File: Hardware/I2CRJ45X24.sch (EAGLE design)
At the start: 129 parts, among them IC1 MCP23017SO, IC2 MCP23017SO, IC3 MCP23017SO, IC4 MCP23017SO, IC5 MCP23017SO, IC6 MCP23017SO, J1 I2C-BREAKOUT, J2 I2C-BREAKOUT, J3 M01-PLAIN, J4 RJ45-X8, J5 RJ45-X8, J6 RJ45-X8

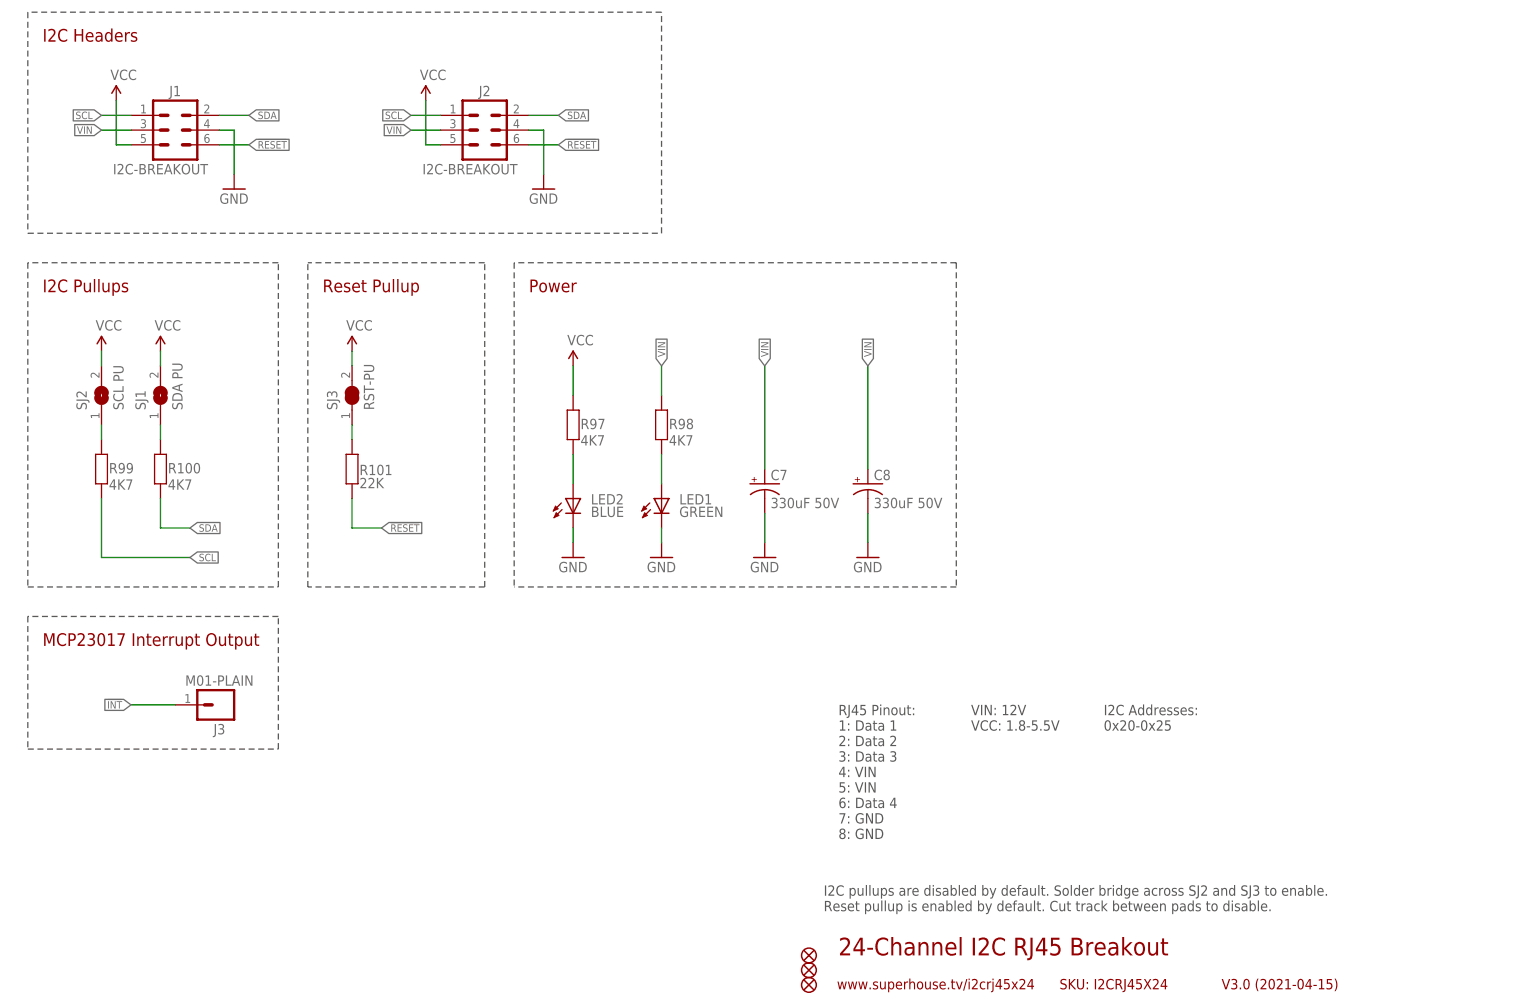
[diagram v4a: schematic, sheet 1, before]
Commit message: Major rework for v3.0 release of all versions.
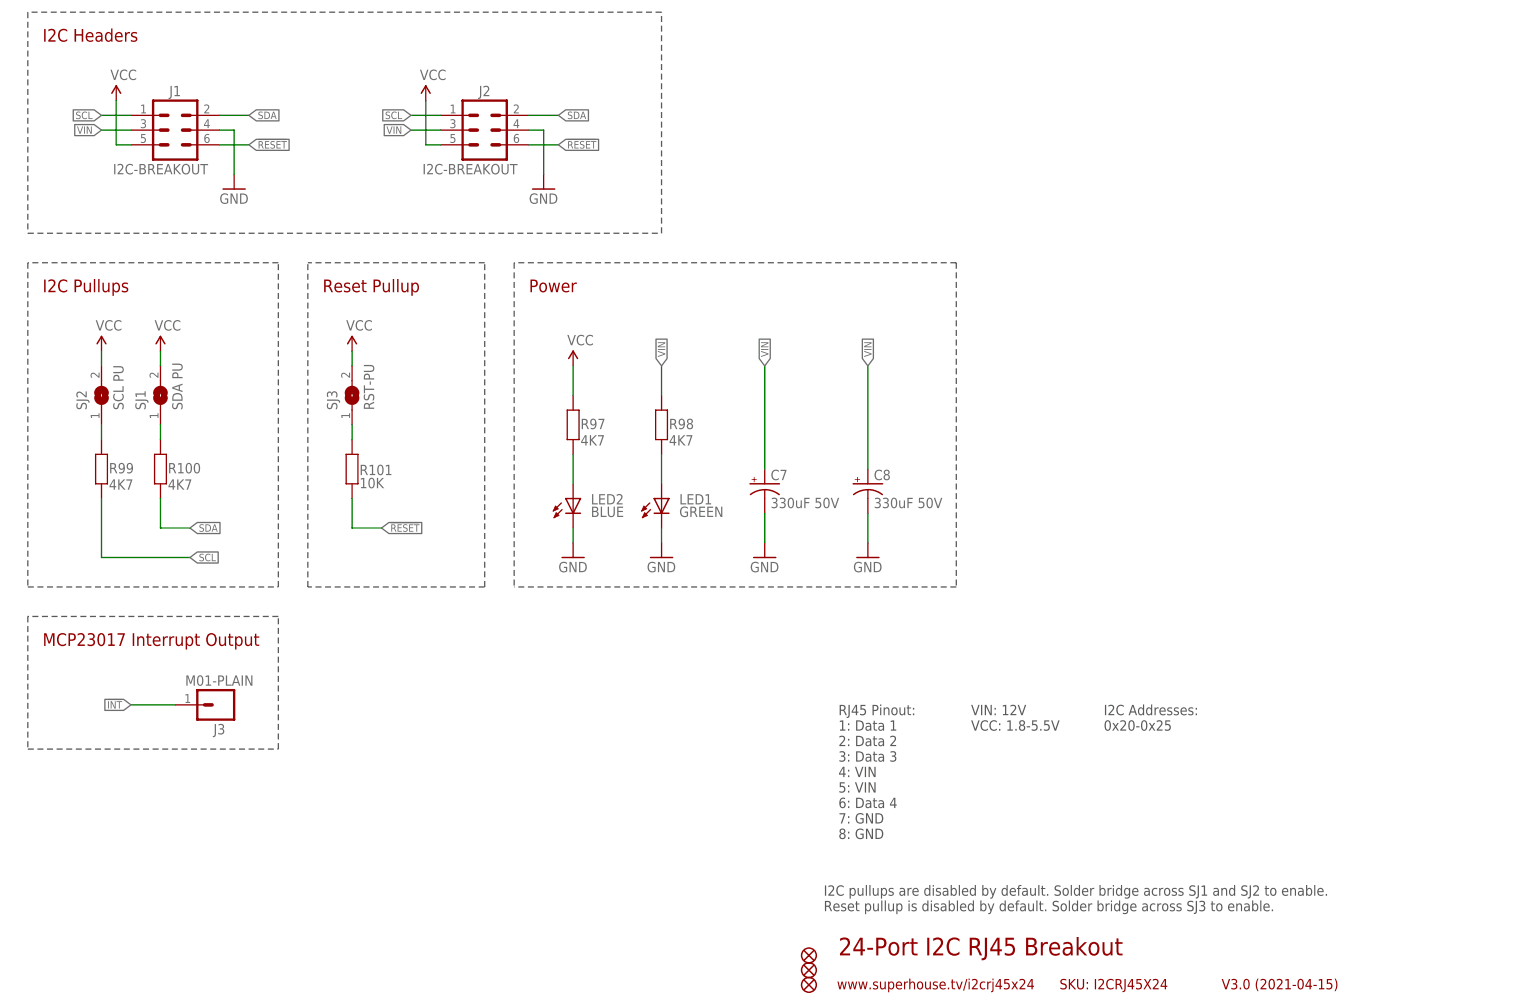
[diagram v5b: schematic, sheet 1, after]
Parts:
- R101: value 22K -> 10K
- SJ3: device SuperHouse-Jumpers:SJC-NORMAL -> SuperHouse-Jumpers:SJ-NORMAL
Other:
- note added: "24-Port I2C RJ45 Breakout"
- note added: "I2C pullups are disabled by default. Solder bridge across SJ1 and SJ2 to enable. Reset pullup is disabled by default. Solder bridge across SJ3 to enable."
- note removed: "24-Channel I2C RJ45 Breakout"
- note removed: "I2C pullups are disabled by default. Solder bridge across SJ2 and SJ3 to enable. Reset pullup is enabled by default. Cut track between pads to disable."
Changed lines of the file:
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@@
 <part name="C3" library="SuperHouse-DiscreteSemi" library_urn="urn:adsk.eagle:library:11768461" deviceset="CAP" device="0805" package3d_urn="urn:adsk.eagle:package:7066318/4" value="10uF"/>
 <part name="C4" library="SuperHouse-DiscreteSemi" library_urn="urn:adsk.eagle:library:11768461" deviceset="CAP" device="0805" package3d_urn="urn:adsk.eagle:package:7066318/4" value="10uF"/>
-<part name="SJ2" library="SuperHouse-Jumpers" library_urn="urn:adsk.eagle:library:12190622" deviceset="SJ" device="-NORMAL" package3d_urn="urn:adsk.eagle:package:7066338/1" value="SCL PU"/>
-<part name="SJ1" library="SuperHouse-Jumpers" library_urn="urn:adsk.eagle:library:12190622" deviceset="SJ" device="-NORMAL" package3d_urn="urn:adsk.eagle:package:7066338/1" value="SDA PU"/>
+<part name="SJ2" library="SuperHouse-Jumpers" library_urn="urn:adsk.eagle:library:12190622" deviceset="SJ" device="-NORMAL" package3d_urn="urn:adsk.eagle:package:7066338/2" value="SCL PU"/>
+<part name="SJ1" library="SuperHouse-Jumpers" library_urn="urn:adsk.eagle:library:12190622" deviceset="SJ" device="-NORMAL" package3d_urn="urn:adsk.eagle:package:7066338/2" value="SDA PU"/>
 <part name="P+8" library="SuperHouse-SupplySymbols" library_urn="urn:adsk.eagle:library:11790503" deviceset="VCC" device=""/>
 <part name="P+9" library="SuperHouse-SupplySymbols" library_urn="urn:adsk.eagle:library:11790503" deviceset="VCC" device=""/>
@@
 <part name="GND14" library="SuperHouse-SupplySymbols" library_urn="urn:adsk.eagle:library:11790503" deviceset="GND" device=""/>
 <part name="GND15" library="SuperHouse-SupplySymbols" library_urn="urn:adsk.eagle:library:11790503" deviceset="GND" device=""/>
-<part name="R101" library="SuperHouse-DiscreteSemi" library_urn="urn:adsk.eagle:library:11768461" deviceset="RESISTOR" device="0603" package3d_urn="urn:adsk.eagle:package:11768543/2" value="22K"/>
+<part name="R101" library="SuperHouse-DiscreteSemi" library_urn="urn:adsk.eagle:library:11768461" deviceset="RESISTOR" device="0603" package3d_urn="urn:adsk.eagle:package:11768543/2" value="10K"/>
 <part name="P+12" library="SuperHouse-SupplySymbols" library_urn="urn:adsk.eagle:library:11790503" deviceset="VCC" device=""/>
-<part name="SJ3" library="SuperHouse-Jumpers" library_urn="urn:adsk.eagle:library:12190622" deviceset="SJC" device="-NORMAL" package3d_urn="urn:adsk.eagle:package:7066342/2" value="RST-PU"/>
+<part name="SJ3" library="SuperHouse-Jumpers" library_urn="urn:adsk.eagle:library:12190622" deviceset="SJ" device="-NORMAL" package3d_urn="urn:adsk.eagle:package:7066338/2" value="RST-PU"/>
 </parts>
 <sheets>
@@
 <plain>
 <frame x1="0" y1="0" x2="248.92" y2="185.42" columns="8" rows="5" layer="94"/>
-<text x="149.86" y="12.7" size="3.048" layer="94">24-Channel I2C RJ45 Breakout</text>
+<text x="149.86" y="12.7" size="3.048" layer="94">24-Port I2C RJ45 Breakout</text>
 <text x="215.9" y="6.858" size="1.778" layer="94">V3.0 (2021-04-15)</text>
 <text x="149.606" y="6.858" size="1.778" layer="94">www.superhouse.tv/i2crj45x24</text>
@@
 <wire x1="119.38" y1="137.16" x2="119.38" y2="175.26" width="0.2032" layer="97" style="longdash"/>
 <wire x1="119.38" y1="175.26" x2="10.16" y2="175.26" width="0.2032" layer="97" style="longdash"/>
-<text x="147.32" y="20.32" size="1.778" layer="97">I2C pullups are disabled by default. Solder bridge across SJ2 and SJ3 to enable.
-Reset pullup is enabled by default. Cut track between pads to disable.</text>
+<text x="147.32" y="20.32" size="1.778" layer="97">I2C pullups are disabled by default. Solder bridge across SJ1 and SJ2 to enable.
+Reset pullup is disabled by default. Solder bridge across SJ3 to enable.</text>
 <wire x1="93.98" y1="132.08" x2="93.98" y2="76.2" width="0.2032" layer="97" style="longdash"/>
 <wire x1="170.18" y1="132.08" x2="93.98" y2="132.08" width="0.2032" layer="97" style="longdash"/>
@@
 <attribute name="VALUE" x="65.024" y="120.396" size="1.778" layer="96"/>
 </instance>
-<instance part="SJ3" gate="G$1" x="66.04" y="109.22" smashed="yes" rot="R90">
+<instance part="SJ3" gate="1" x="66.04" y="109.22" smashed="yes" rot="R90">
 <attribute name="NAME" x="63.5" y="106.68" size="1.778" layer="95" rot="R90"/>
 <attribute name="VALUE" x="69.85" y="106.68" size="1.778" layer="96" rot="R90"/>
@@
 <segment>
 <pinref part="P+12" gate="1" pin="VCC"/>
-<pinref part="SJ3" gate="G$1" pin="2"/>
+<pinref part="SJ3" gate="1" pin="2"/>
 <wire x1="66.04" y1="114.3" x2="66.04" y2="116.84" width="0.1524" layer="91"/>
 </segment>
@@
 <segment>
 <pinref part="R101" gate="G$1" pin="2"/>
-<pinref part="SJ3" gate="G$1" pin="1"/>
+<pinref part="SJ3" gate="1" pin="1"/>
 <wire x1="66.04" y1="101.6" x2="66.04" y2="104.14" width="0.1524" layer="91"/>
 </segment>

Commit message: Began replacement of discrete resistors with resistor arrays.
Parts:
- removed R1, R10, R11, R12, R13, R14, R15, R16, R2, R3, R4, R5, R6, R7, R8, R9: 1K, SuperHouse-DiscreteSemi:RESISTOR0603
- added RN1, RN2, RN3, RN4: 1K, SuperHouse-DiscreteSemi:4R-NCAY16
- added RN5, RN6, RN7, RN8: (no value), SuperHouse-DiscreteSemi:4R-NCAY16
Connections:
- net 1A1: now also RN1D.2, RN5D.1; no longer R1.2
- net 1A2: now also RN1C.2, RN5C.1; no longer R3.2
- net 1A3: now also RN1B.2, RN5B.1; no longer R2.2
- net 1A6: now also RN1A.2, RN5A.1; no longer R4.2
- net 1B1: now also RN3D.2, RN7D.1; no longer R15.2
- net 1B2: now also RN3C.2, RN7C.1; no longer R13.2
- net 1B3: now also RN3B.2, RN7B.1; no longer R11.2
- net 1B6: now also RN3A.2, RN7A.1; no longer R9.2
- net 1E1: now also RN2D.2, RN6D.1; no longer R7.2
- net 1E2: now also RN2C.2, RN6C.1; no longer R6.2
- net 1E3: now also RN2B.2, RN6B.1; no longer R5.2
- net 1E6: now also RN2A.2, RN6A.1; no longer R8.2
- net 1F1: now also RN4D.2, RN8D.1; no longer R16.2
- net 1F2: now also RN4C.2, RN8C.1; no longer R14.2
- net 1F3: now also RN4B.2, RN8B.1; no longer R12.2
- net 1F6: now also RN4A.2, RN8A.1; no longer R10.2
- net GPA0-1: now also RN1D.1; no longer R1.1
- net GPA1-1: now also RN1C.1; no longer R3.1
- net GPA2-1: now also RN1B.1; no longer R2.1
- net GPA3-1: now also RN1A.1; no longer R4.1
- net GPA4-1: now also RN2D.1; no longer R7.1
- net GPA5-1: now also RN2C.1; no longer R6.1
- net GPA6-1: now also RN2B.1; no longer R5.1
- net GPA7-1: now also RN2A.1; no longer R8.1
- net GPB0-1: now also RN3D.1; no longer R15.1
- net GPB1-1: now also RN3C.1; no longer R13.1
- net GPB2-1: now also RN3B.1; no longer R11.1
- net GPB3-1: now also RN3A.1; no longer R9.1
- net GPB4-1: now also RN4D.1; no longer R16.1
- net GPB5-1: now also RN4C.1; no longer R14.1
- net GPB6-1: now also RN4B.1; no longer R12.1
- net GPB7-1: now also RN4A.1; no longer R10.1
- net VCC: now also RN5A.2, RN5B.2, RN5C.2, RN5D.2, RN6A.2, RN6B.2, RN6C.2, RN6D.2, RN7A.2, RN7B.2, RN7C.2, RN7D.2, RN8A.2, RN8B.2, RN8C.2, RN8D.2
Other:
- moved on the sheet: C1, C2, IC1, IC2, J4, R17, R18, R19, R20, R21, R22, R23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

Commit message: Progress on converting resistors to arrays and adding pullups.
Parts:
- removed R17, R18, R19, R20, R21, R22, R23, R24, R25, R26, R27, R28, R29, R30, R31, R32, R33, R34, R35, R36, R37, R38, R41, R42, R43, R44, R45, R46, R47, R48, R49, R50, R51, R52, R53, R54, R55, R56, R57, R58, R59, R60, R61, R62, R63, R64, R65, R66: 1K, SuperHouse-DiscreteSemi:RESISTOR0603
- added RN10, RN11, RN12, RN17, RN18, RN19, RN20, RN25, RN26, RN27, RN28, RN9: 1K, SuperHouse-DiscreteSemi:4R-NCAY16
- added RN13, RN14, RN15, RN16, RN21, RN22, RN23, RN24, RN29, RN30, RN31, RN32: 10K, SuperHouse-DiscreteSemi:4R-NCAY16
- RN5, RN6, RN7, RN8: value (none) -> 10K
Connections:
- net 1C1: now also RN13D.1, RN9D.2; no longer R17.2
- net 1C2: now also RN13C.1, RN9C.2; no longer R19.2
- net 1C3: now also RN13B.1, RN9B.2; no longer R18.2
- net 1C6: now also RN13A.1, RN9A.2; no longer R20.2
- net 1D1: now also RN11D.2, RN15D.1; no longer R31.2
- net 1D2: now also RN11C.2, RN15C.1; no longer R29.2
- net 1D3: now also RN11B.2, RN15B.1; no longer R27.2
- net 1D6: now also RN11A.2, RN15A.1; no longer R25.2
- net 1G1: now also RN10D.2, RN14D.1; no longer R23.2
- net 1G2: now also RN10C.2, RN14C.1; no longer R22.2
- net 1G3: now also RN10B.2, RN14B.1; no longer R21.2
- net 1G6: now also RN10A.2, RN14A.1; no longer R24.2
- net 1H1: now also RN12D.2, RN16D.1; no longer R32.2
- net 1H2: now also RN12C.2, RN16C.1; no longer R30.2
- net 1H3: now also RN12B.2, RN16B.1; no longer R28.2
- net 1H6: now also RN12A.2, RN16A.1; no longer R26.2
- net 2A1: now also RN17D.2, RN21D.1; no longer R33.2
- net 2A2: now also RN17C.2, RN21C.1; no longer R35.2
- net 2A3: now also RN17B.2, RN21B.1; no longer R34.2
- net 2A6: now also RN17A.2, RN21A.1; no longer R36.2
- net 2B1: now also RN19D.2, RN23D.1; no longer R49.2
- net 2B2: now also RN19C.2, RN23C.1; no longer R47.2
- net 2B3: now also RN19B.2, RN23B.1; no longer R45.2
- net 2B6: now also RN19A.2, RN23A.1; no longer R43.2
- net 2C1: now also RN25D.2, RN29D.1; no longer R51.2
- net 2C2: now also RN25C.2, RN29C.1; no longer R53.2
- net 2C3: now also RN25B.2, RN29B.1; no longer R52.2
- net 2C6: now also RN25A.2, RN29A.1; no longer R54.2
- net 2D1: now also RN27D.2, RN31D.1; no longer R65.2
- net 2D2: now also RN27C.2, RN31C.1; no longer R63.2
- net 2D3: now also RN27B.2, RN31B.1; no longer R61.2
- net 2D6: now also RN27A.2, RN31A.1; no longer R59.2
- net 2E1: now also RN18D.2, RN22D.1; no longer R41.2
- net 2E2: now also RN18C.2, RN22C.1; no longer R38.2
- net 2E3: now also RN18B.2, RN22B.1; no longer R37.2
- net 2E6: now also RN18A.2, RN22A.1; no longer R42.2
- net 2F1: now also RN20D.2, RN24D.1; no longer R50.2
- net 2F2: now also RN20C.2, RN24C.1; no longer R48.2
- net 2F3: now also RN20B.2, RN24B.1; no longer R46.2
- net 2F6: now also RN20A.2, RN24A.1; no longer R44.2
- net 2G1: now also RN26D.2, RN30D.1; no longer R57.2
- net 2G2: now also RN26C.2, RN30C.1; no longer R56.2
- net 2G3: now also RN26B.2, RN30B.1; no longer R55.2
- net 2G6: now also RN26A.2, RN30A.1; no longer R58.2
- net 2H1: now also RN28D.2, RN32D.1; no longer R66.2
- net 2H2: now also RN28C.2, RN32C.1; no longer R64.2
- net 2H3: now also RN28B.2, RN32B.1; no longer R62.2
- net 2H6: now also RN28A.2, RN32A.1; no longer R60.2
- net GPA0-2: now also RN9D.1; no longer R17.1
- net GPA0-3: now also RN17D.1; no longer R33.1
- net GPA0-4: now also RN25D.1; no longer R51.1
- net GPA1-2: now also RN9C.1; no longer R19.1
- net GPA1-3: now also RN17C.1; no longer R35.1
- net GPA1-4: now also RN25C.1; no longer R53.1
- net GPA2-2: now also RN9B.1; no longer R18.1
- net GPA2-3: now also RN17B.1; no longer R34.1
- net GPA2-4: now also RN25B.1; no longer R52.1
- net GPA3-2: now also RN9A.1; no longer R20.1
- net GPA3-3: now also RN17A.1; no longer R36.1
- net GPA3-4: now also RN25A.1; no longer R54.1
- net GPA4-2: now also RN10D.1; no longer R23.1
- net GPA4-3: now also RN18D.1; no longer R41.1
- net GPA4-4: now also RN26D.1; no longer R57.1
- net GPA5-2: now also RN10C.1; no longer R22.1
- net GPA5-3: now also RN18C.1; no longer R38.1
- net GPA5-4: now also RN26C.1; no longer R56.1
- net GPA6-2: now also RN10B.1; no longer R21.1
- net GPA6-3: now also RN18B.1; no longer R37.1
- net GPA6-4: now also RN26B.1; no longer R55.1
- net GPA7-2: now also RN10A.1; no longer R24.1
- net GPA7-3: now also RN18A.1; no longer R42.1
- net GPA7-4: now also RN26A.1; no longer R58.1
- net GPB0-2: now also RN11D.1; no longer R31.1
- net GPB0-3: now also RN19D.1; no longer R49.1
- net GPB0-4: now also RN27D.1; no longer R65.1
- net GPB1-2: now also RN11C.1; no longer R29.1
- net GPB1-3: now also RN19C.1; no longer R47.1
- net GPB1-4: now also RN27C.1; no longer R63.1
- net GPB2-2: now also RN11B.1; no longer R27.1
- net GPB2-3: now also RN19B.1; no longer R45.1
- net GPB2-4: now also RN27B.1; no longer R61.1
- net GPB3-2: now also RN11A.1; no longer R25.1
- net GPB3-3: now also RN19A.1; no longer R43.1
- net GPB3-4: now also RN27A.1; no longer R59.1
- net GPB4-2: now also RN12D.1; no longer R32.1
- net GPB4-3: now also RN20D.1; no longer R50.1
- net GPB4-4: now also RN28D.1; no longer R66.1
- net GPB5-2: now also RN12C.1; no longer R30.1
- net GPB5-3: now also RN20C.1; no longer R48.1
- net GPB5-4: now also RN28C.1; no longer R64.1
- net GPB6-2: now also RN12B.1; no longer R28.1
- net GPB6-3: now also RN20B.1; no longer R46.1
- net GPB6-4: now also RN28B.1; no longer R62.1
- net GPB7-2: now also RN12A.1; no longer R26.1
- net GPB7-3: now also RN20A.1; no longer R44.1
- net GPB7-4: now also RN28A.1; no longer R60.1
- net VCC: now also RN13A.2, RN13B.2, RN13C.2, RN13D.2, RN14A.2, RN14B.2, RN14C.2, RN14D.2, RN15A.2, RN15B.2, RN15C.2, RN15D.2, RN16A.2, RN16B.2, RN16C.2, RN16D.2, RN21A.2, RN21B.2, RN21C.2, RN21D.2, RN22A.2, RN22B.2, RN22C.2, RN22D.2, RN23A.2, RN23B.2, RN23C.2, RN23D.2, RN24A.2, RN24B.2, RN24C.2, RN24D.2, RN29A.2, RN29B.2, RN29C.2, RN29D.2, RN30A.2, RN30B.2, RN30C.2, RN30D.2, RN31A.2, RN31B.2, RN31C.2, RN31D.2, RN32A.2, RN32B.2, RN32C.2, RN32D.2
